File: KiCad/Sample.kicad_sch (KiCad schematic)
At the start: 4 parts, among them J1 Conn_01x04, U1 "74LS175", U2 74LS86, X1 CXO_DIP8

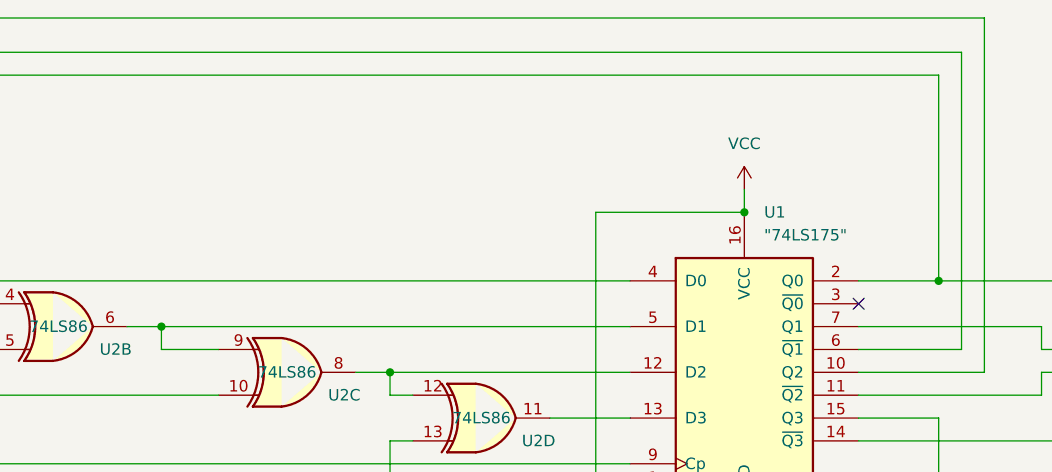
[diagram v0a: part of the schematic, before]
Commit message: Code now builds and dumps a tree of ModelNodes
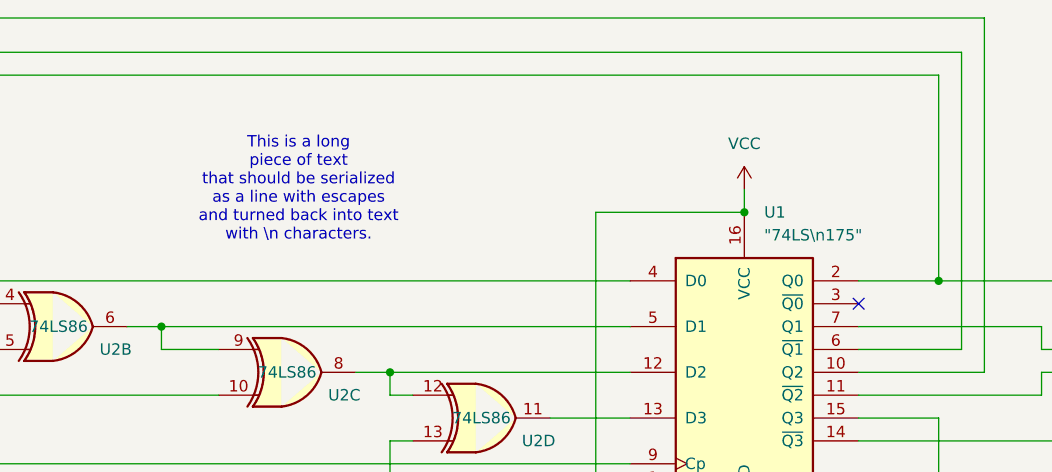
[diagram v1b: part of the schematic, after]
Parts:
- U1: value "74LS175" -> "74LS\n175"
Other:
- note added: "This is a long piece of text that should be serialized as a line with escapes and turned back into text with \n characters."
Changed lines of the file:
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@@
+		)
+	)
+	(text "This is a long\npiece of text\nthat should be serialized\nas a line with escapes\nand turned back into text\nwith \\n characters."
+		(exclude_from_sim no)
+		(at 111.76 55.88 0)
+		(effects
+			(font
+				(size 1.27 1.27)
+			)
 		)
 	)
@@
 			)
 		)
-		(property "Value" "\"74LS175\""
+		(property "Value" "\"74LS\\n175\""
 			(at 163.4841 60.96 0)
 			(effects

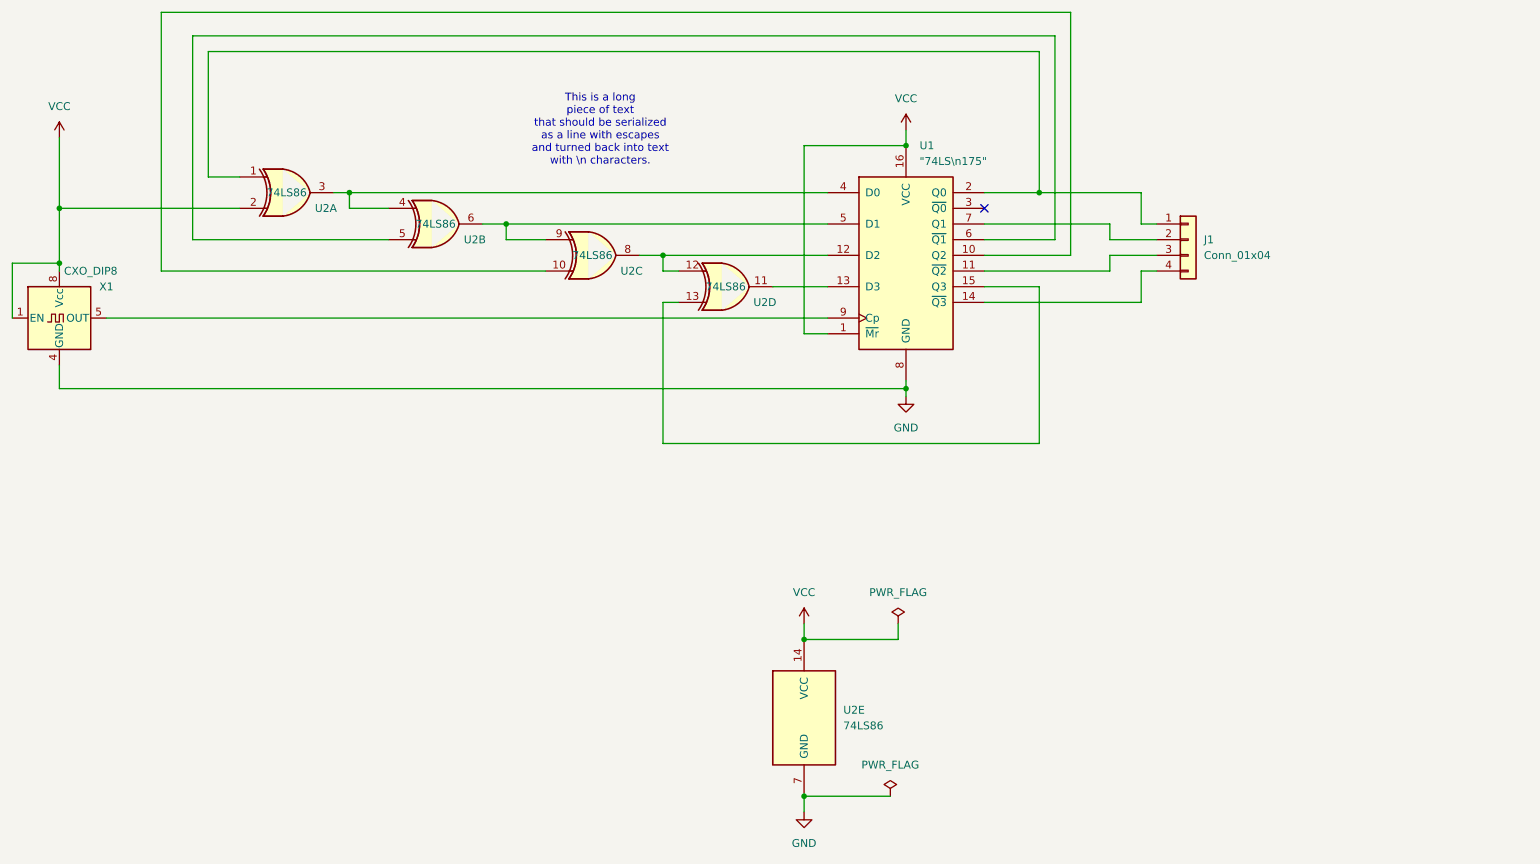
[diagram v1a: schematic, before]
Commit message: Ongoing development of schematic and transpiler
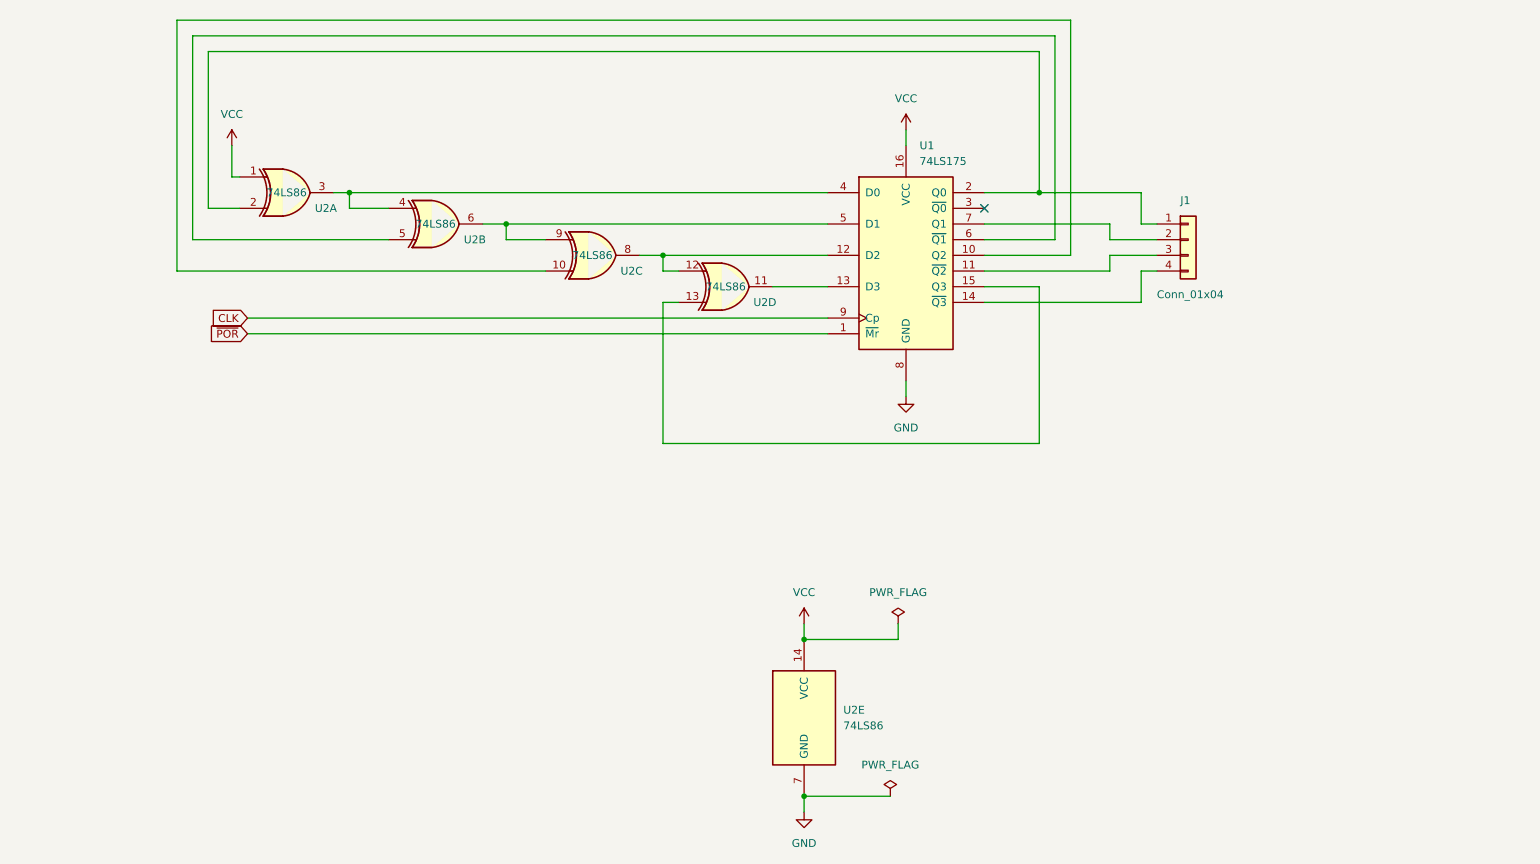
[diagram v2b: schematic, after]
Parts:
- removed X1: CXO_DIP8, Oscillator:Oscillator_DIP-8, symbol Oscillator:CXO_DIP8
- U1: value "74LS\n175" -> 74LS175
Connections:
- net VCC: now also U2.1; no longer U1.1 (~{Mr}), U2.2
- net at J1.1 (Pin_1), U1.2 (Q0): now also U2.2; no longer U2.1
- net CLK: now reaches U1.9 (Cp)
- new net ~{POR}: U1.1 (~{Mr})
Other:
- note removed: "This is a long piece of text that should be serialized as a line with escapes and turned back into text with \n characters."
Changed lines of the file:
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@@
-	)
-	(junction
-		(at 161.29 97.79)
-		(diameter 0)
-		(color 0 0 0 0)
 	)
 	(junction
@@
 	)
 	(junction
-		(at 24.13 77.47)
-		(diameter 0)
-		(color 0 0 0 0)
-	)
-	(junction
-		(at 161.29 58.42)
-		(diameter 0)
-		(color 0 0 0 0)
-	)
-	(junction
-		(at 24.13 68.58)
-		(diameter 0)
-		(color 0 0 0 0)
-	)
-	(junction
 		(at 144.78 138.43)
 		(diameter 0)
@@
 	(wire
 		(pts
-			(xy 24.13 77.47) (xy 24.13 78.74)
-		)
-		(stroke
-			(width 0)
-			(type default)
-		)
-	)
-	(wire
-		(pts
-			(xy 161.29 97.79) (xy 161.29 96.52)
+			(xy 161.29 96.52) (xy 161.29 99.06)
 		)
 		(stroke
@@
 	(wire
 		(pts
-			(xy 24.13 68.58) (xy 24.13 77.47)
+			(xy 52.07 58.42) (xy 52.07 63.5)
 		)
 		(stroke
@@
 	(wire
 		(pts
-			(xy 31.75 86.36) (xy 148.59 86.36)
+			(xy 54.61 86.36) (xy 148.59 86.36)
 		)
 		(stroke
@@
 	(wire
 		(pts
-			(xy 24.13 57.15) (xy 24.13 68.58)
-		)
-		(stroke
-			(width 0)
-			(type default)
-		)
-	)
-	(wire
-		(pts
 			(xy 144.78 135.89) (xy 144.78 138.43)
 		)
@@
 	(wire
 		(pts
-			(xy 161.29 99.06) (xy 161.29 97.79)
-		)
-		(stroke
-			(width 0)
-			(type default)
-		)
-	)
-	(wire
-		(pts
-			(xy 148.59 88.9) (xy 144.78 88.9)
-		)
-		(stroke
-			(width 0)
-			(type default)
-		)
-	)
-	(wire
-		(pts
-			(xy 144.78 58.42) (xy 161.29 58.42)
+			(xy 48.26 68.58) (xy 53.34 68.58)
 		)
 		(stroke
@@
 	(wire
 		(pts
-			(xy 24.13 68.58) (xy 53.34 68.58)
-		)
-		(stroke
-			(width 0)
-			(type default)
-		)
-	)
-	(wire
-		(pts
 			(xy 194.31 78.74) (xy 194.31 76.2)
 		)
@@
 	(wire
 		(pts
-			(xy 40.64 36.83) (xy 40.64 78.74)
+			(xy 43.18 38.1) (xy 43.18 78.74)
 		)
 		(stroke
@@
 	(wire
 		(pts
+			(xy 53.34 63.5) (xy 52.07 63.5)
+		)
+		(stroke
+			(width 0)
+			(type default)
+		)
+	)
+	(wire
+		(pts
 			(xy 121.92 76.2) (xy 148.59 76.2)
 		)
@@
 	(wire
 		(pts
+			(xy 54.61 88.9) (xy 148.59 88.9)
+		)
+		(stroke
+			(width 0)
+			(type default)
+		)
+	)
+	(wire
+		(pts
 			(xy 144.78 138.43) (xy 160.02 138.43)
 		)
@@
 	(wire
 		(pts
-			(xy 144.78 88.9) (xy 144.78 58.42)
-		)
-		(stroke
-			(width 0)
-			(type default)
-		)
-	)
-	(wire
-		(pts
 			(xy 185.42 73.66) (xy 185.42 40.64)
 		)
@@
 	(wire
 		(pts
-			(xy 24.13 97.79) (xy 161.29 97.79)
-		)
-		(stroke
-			(width 0)
-			(type default)
-		)
-	)
-	(wire
-		(pts
 			(xy 124.46 78.74) (xy 121.92 78.74)
 		)
@@
 	(wire
 		(pts
-			(xy 48.26 63.5) (xy 53.34 63.5)
-		)
-		(stroke
-			(width 0)
-			(type default)
-		)
-	)
-	(wire
-		(pts
-			(xy 40.64 78.74) (xy 102.87 78.74)
-		)
-		(stroke
-			(width 0)
-			(type default)
-		)
-	)
-	(wire
-		(pts
-			(xy 187.96 36.83) (xy 40.64 36.83)
+			(xy 43.18 78.74) (xy 102.87 78.74)
+		)
+		(stroke
+			(width 0)
+			(type default)
+		)
+	)
+	(wire
+		(pts
+			(xy 187.96 38.1) (xy 43.18 38.1)
 		)
 		(stroke
@@
 	(wire
 		(pts
-			(xy 24.13 93.98) (xy 24.13 97.79)
-		)
-		(stroke
-			(width 0)
-			(type default)
-		)
-	)
-	(wire
-		(pts
 			(xy 199.39 78.74) (xy 201.93 78.74)
 		)
@@
 	(wire
 		(pts
-			(xy 48.26 43.18) (xy 48.26 63.5)
-		)
-		(stroke
-			(width 0)
-			(type default)
-		)
-	)
-	(wire
-		(pts
 			(xy 121.92 83.82) (xy 124.46 83.82)
 		)
@@
 	(wire
 		(pts
-			(xy 16.51 86.36) (xy 16.51 77.47)
-		)
-		(stroke
-			(width 0)
-			(type default)
-		)
-	)
-	(wire
-		(pts
 			(xy 194.31 71.12) (xy 194.31 73.66)
 		)
@@
 	(wire
 		(pts
-			(xy 16.51 77.47) (xy 24.13 77.47)
-		)
-		(stroke
-			(width 0)
-			(type default)
-		)
-	)
-	(wire
-		(pts
 			(xy 173.99 76.2) (xy 187.96 76.2)
 		)
@@
 	(wire
 		(pts
-			(xy 187.96 76.2) (xy 187.96 36.83)
+			(xy 48.26 43.18) (xy 48.26 68.58)
+		)
+		(stroke
+			(width 0)
+			(type default)
+		)
+	)
+	(wire
+		(pts
+			(xy 187.96 76.2) (xy 187.96 38.1)
 		)
 		(stroke
@@
 		)
 	)
-	(text "This is a long\npiece of text\nthat should be serialized\nas a line with escapes\nand turned back into text\nwith \\n characters."
-		(exclude_from_sim no)
-		(at 111.76 55.88 0)
+	(global_label "~{POR}"
+		(shape input)
+		(at 54.61 88.9 180)
+		(fields_autoplaced yes)
 		(effects
 			(font
 				(size 1.27 1.27)
+			)
+			(justify right)
+		)
+		(property "Intersheetrefs" "${INTERSHEET_REFS}"
+			(at 47.7543 88.9 0)
+			(effects
+				(font
+					(size 1.27 1.27)
+				)
+				(justify right)
+				(hide yes)
+			)
+		)
+	)
+	(global_label "CLK"
+		(shape input)
+		(at 54.61 86.36 180)
+		(fields_autoplaced yes)
+		(effects
+			(font
+				(size 1.27 1.27)
+			)
+			(justify right)
+		)
+		(property "Intersheetrefs" "${INTERSHEET_REFS}"
+			(at 48.0567 86.36 0)
+			(effects
+				(font
+					(size 1.27 1.27)
+				)
+				(justify right)
+				(hide yes)
 			)
 		)
@@
 	(symbol
 		(lib_id "power:VCC")
-		(at 24.13 57.15 0)
+		(at 52.07 58.42 0)
 		(unit 1)
 		(exclude_from_sim no)
@@
 		(fields_autoplaced yes)
 		(property "Reference" "#PWR05"
-			(at 24.13 60.96 0)
+			(at 52.07 62.23 0)
 			(effects
 				(font
@@
 		)
 		(property "Value" "VCC"
-			(at 24.13 52.07 0)
+			(at 52.07 53.34 0)
 			(effects
 				(font
@@
 		)
 		(property "Footprint" ""
-			(at 24.13 57.15 0)
+			(at 52.07 58.42 0)
 			(effects
 				(font
@@
 		)
 		(property "Datasheet" ""
-			(at 24.13 57.15 0)
+			(at 52.07 58.42 0)
 			(effects
 				(font
@@
 		)
 		(property "Description" "Power symbol creates a global label with name \"VCC\""
-			(at 24.13 57.15 0)
+			(at 52.07 58.42 0)
 			(effects
 				(font
@@
 		(on_board yes)
 		(dnp no)
-		(fields_autoplaced yes)
 		(property "Reference" "J1"
-			(at 209.55 73.6599 0)
+			(at 205.74 67.31 0)
 			(effects
 				(font
@@
 		)
 		(property "Value" "Conn_01x04"
-			(at 209.55 76.1999 0)
+			(at 201.93 82.55 0)
 			(effects
 				(font
@@
 			)
 		)
-		(property "Value" "\"74LS\\n175\""
+		(property "Value" "74LS175"
 			(at 163.4841 60.96 0)
 			(effects
@@
 					(unit 1)
 				)
-			)
-		)
-	)
-	(symbol
-		(lib_id "Oscillator:CXO_DIP8")
-		(at 24.13 86.36 0)
-		(unit 1)
-		(exclude_from_sim no)
-		(in_bom yes)
-		(on_board yes)
-		(dnp no)
-		(property "Reference" "X1"
-			(at 31.75 81.28 0)
-			(effects
-				(font
-					(size 1.27 1.27)
-				)
-			)
-		)
-		(property "Value" "CXO_DIP8"
-			(at 29.21 78.74 0)
-			(effects
-				(font
-					(size 1.27 1.27)
-				)
-			)
-		)
-		(property "Footprint" "Oscillator:Oscillator_DIP-8"
-			(at 35.56 95.25 0)
-			(effects
-				(font
-					(size 1.27 1.27)
-				)
-				(hide yes)
-			)
-		)
-		(property "Datasheet" "http://cdn-reichelt.de/documents/datenblatt/B400/OSZI.pdf"
-			(at 21.59 86.36 0)
-			(effects
-				(font
-					(size 1.27 1.27)
-				)
-				(hide yes)
-			)
-		)
-		(property "Description" "Crystal Clock Oscillator, DIP8-style metal package"
-			(at 24.13 86.36 0)
-			(effects
-				(font
-					(size 1.27 1.27)
-				)
-				(hide yes)
-			)
-		)
-		(pin "1"
-		)
-		(pin "4"
-		)
-		(pin "5"
-		)
-		(pin "8"
-		)
-		(instances
-			(project "Sample"
-				(path "/9e6cafd0-a629-4042-bd25-6234388dab21"
-					(reference "X1")
-					(unit 1)
-				)

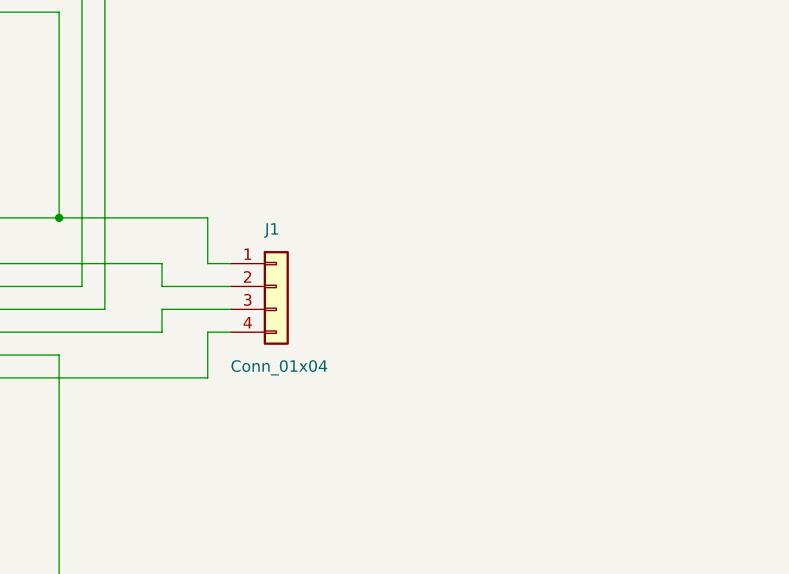
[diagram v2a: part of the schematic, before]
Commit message: Add a bus to the sample data and hack on the code a bit
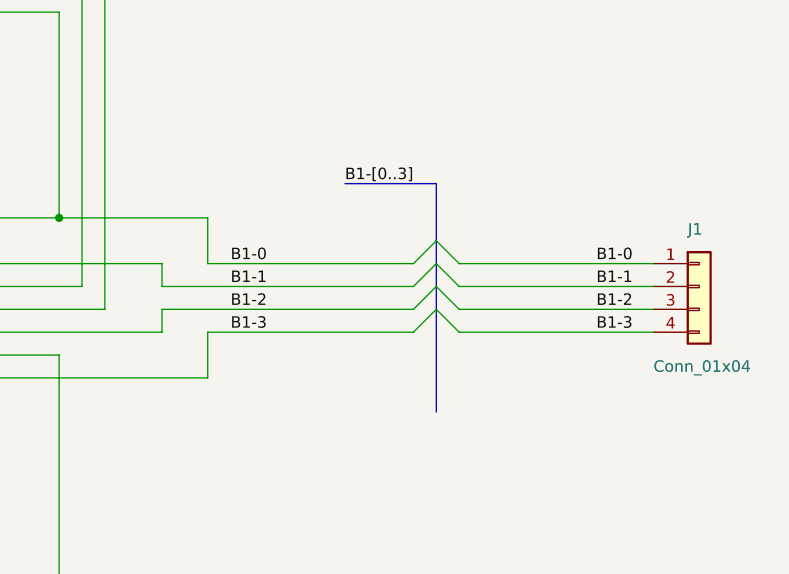
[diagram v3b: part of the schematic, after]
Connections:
- net B1-0: now reaches J1.1 (Pin_1), U1.2 (Q0), U2.2
- net B1-1: now reaches J1.2 (Pin_2), U1.7 (Q1)
- net B1-2: now reaches J1.3 (Pin_3), U1.11 (~{Q2})
- net B1-3: now reaches J1.4 (Pin_4), U1.14 (~{Q3})
